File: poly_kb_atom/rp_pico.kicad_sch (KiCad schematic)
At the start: 44 parts, among them SW2 TSA343G00-250J2, SW3 TSA343G00-250J2, U1 TD6811, U10 RP2040, U9 W25Q64JVSSIQ, Y1 TAXM12M4RFBCCT2T

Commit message: Current production version of right side and added STLs
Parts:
- C15, C16, C17, C18, C19, C20, C21, C22, C23, C7, C9: LCSC C1525 -> (none); MPN CL05B104KO5NNNC -> C1525
- C24, C25: LCSC C52923 -> (none); MPN CL05A105KA5NQNC -> C52923
- C26, C4, C6: LCSC C15850 -> (none); MPN CL21A106KAYNNNE -> C15850
- C3, C8: LCSC C1557 -> (none); MPN 0402CG270J500NT -> C1557
- C5: LCSC C1653 -> (none); MPN CL10C220JB8NNNC -> C1653
- CR1: LCSC C8598 -> (none); MPN B5819W SL -> C8598
- D1: LCSC C84256 -> (none); MPN NCD0805R1 -> C84256
- L2: LCSC C2836880 -> (none); MPN MCS0530-4R7MN2 -> C2836880
- R14: LCSC C23150 -> (none); MPN (none) -> C25822
- R15, R20: LCSC C25744 -> (none); MPN (none) -> C25744
- R16, R19: LCSC C21190 -> (none); MPN (none) -> C21190
- R17: LCSC C22807 -> (none); MPN (none) -> C22807
- R18: LCSC C25091 -> (none); MPN (none) -> C25091
- R21: value 1K 0603 -> 1K 0402; LCSC C21190 -> (none); MPN (none) -> C11702
- R22, R23: LCSC C25190 -> (none); MPN (none) -> C25190
- R7, R9: LCSC C25905 -> (none); MPN (none) -> C25905
- R8: LCSC C25908 -> (none); MPN (none) -> C25908
- SW2, SW3: value TSA343G00-250J2 -> EVQPUC02K; LCSC C79174 -> (none); MPN EVQPUC02K -> C79174
- U1: LCSC C189486 -> (none); MPN TD6811 -> C189486
- U10: LCSC C2040 -> (none); MPN (none) -> C2040
- U9: LCSC C179171 -> (none); MPN W25Q64JVSSIQ -> C179171
- USB1: LCSC C165948 -> (none); MPN TYPE-C-31-M-12 -> C165948
- Y1: LCSC C133337 -> (none); MPN TAXM12M4RFBCCT2T -> C133337

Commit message: Backup before moving to Kicad7
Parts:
- removed C7: 100nF 0402 16V, Capacitor_SMD:C_0402_1005Metric, symbol Device:C_Small
- removed CR1: B5819W SL, Diode_SMD:D_SOD-123, symbol rpi-pico-debugger-shoe-rescue:MBR120VLSFT1G-2021-05-12_00-49-18
- removed R18: 220 0402, Resistor_SMD:R_0402_1005Metric, symbol Device:R
- added D2: ESD5Z5V0, Diode_SMD:D_SOD-523, symbol Diode:SMF6V0A
- added F2: SMD0805-050-16V, Fuse:Fuse_1206_3216Metric, symbol Device:Fuse
- added FB3: GZ2012D601TF, Inductor_SMD:L_0805_2012Metric, symbol Device:FerriteBead_Small
- added R18: 10M 0603, Resistor_SMD:R_0603_1608Metric, symbol Device:R_Small
- added R24: 2M2 0603, Resistor_SMD:R_0603_1608Metric, symbol Device:R_Small
- added U13: TPD4E05U06DQAR, poly_kb:USON-10, symbol acheron_Symbols:TPD4E05U06DQAR
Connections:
- net GND: now also SW2.1, D2.2 (A2), FB3.2, R24.2, U13.3 (GND), U13.8 (GND); no longer SW2.2
- net USB_D+: now also U13.1 (IO1), U13.10 (NC), U13.4 (D2+), U13.7 (NC)
- net USB_D-: now also U13.2 (IO2), U13.5 (D2-), U13.6 (NC), U13.9 (NC)
- net VBUS: now also D2.1 (A1), F2.1; no longer R8.1
- net VSYS: now also R8.1, F2.2
- net ~{USB_BOOT}: now also SW2.2; no longer SW2.1
- net at USB1.13 (SHIELD): now also FB3.1
- net at C5.2, R14.1, R17.2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: now also R18.1
- new net: R18.2, R24.1
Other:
- note added: "ESD"
- note added: "If USB is the only power source it is safe to use VBUS=VSYS, otherwise we need no insert a Schottky barrier diode in-between."
- note added: "R1"
- note added: "R2"
- note added: "Vout = 0.6*(1+R2/R1)"
- moved on the sheet: C9, R14, R15, R17, R20, R21, R8, SW2, U9

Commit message: Revised Rev2
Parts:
- removed U1: TD6811, Package_TO_SOT_SMD:TSOT-23-5, symbol poly_kb:TD6811
- added U2: TD6811, Package_TO_SOT_SMD:TSOT-23-5, symbol poly_kb:TD6811
- F2: value SMD0805-050-16V -> 2920L030DR; footprint Fuse:Fuse_1206_3216Metric -> Fuse:Fuse_2920_7451Metric; LCSC Part Number C2833485 -> (none); MPN (none) -> C207081; Manufacturer TECHFUSE -> (none); Manufacturer Part Number SMD0805-050-16V -> (none); Package F0805 -> (none)
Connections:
- net GND: now also U2.2 (GND)
- net VSYS: now also U2.1 (RUN), U2.4 (VDD)
- net at L2.1: now also U2.3 (SW)
- net at C5.2, R14.1, R17.2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: now also U2.5 (FB)
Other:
- note added: "IHold = 300mA, ITrip = 600 mA"

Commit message: Right side: Production version Rev2
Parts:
- removed U9: W25Q64JVSSIQ, Package_SO:SOIC-8_5.275x5.275mm_P1.27mm, symbol rpi-pico-debugger-shoe-rescue:W25Q16JVSSIQ-W25Q16JVSSIQ
- added U9: W25Q64JVXGIQ, SON80P400X400X50-9N, symbol Winbond Flash:W25Q64JVXGIQ
- D1: value Red 0805 -> Red 0805 C84256
- U13: Package uSON-10 -> (none)
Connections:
- net 3V3: now also U9.8 (VCC)
- net GND: now also U9.4 (GND), U9.9 (EP)
- net QSPI_SCLK: now also U9.6 (CLK)
- net QSPI_SD0: now also U9.5 (DI(IO0))
- net QSPI_SD1: now also U9.2 (DO(IO1))
- net QSPI_SD2: now also U9.3 (~{WP(IO2}))
- net QSPI_SD3: now also U9.7 (~{HOLD_OR_}RESET_(IO3))
- net QSPI_SS: now also U9.1 (~{CS})
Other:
- moved on the sheet: C9, R20, R21, SW2

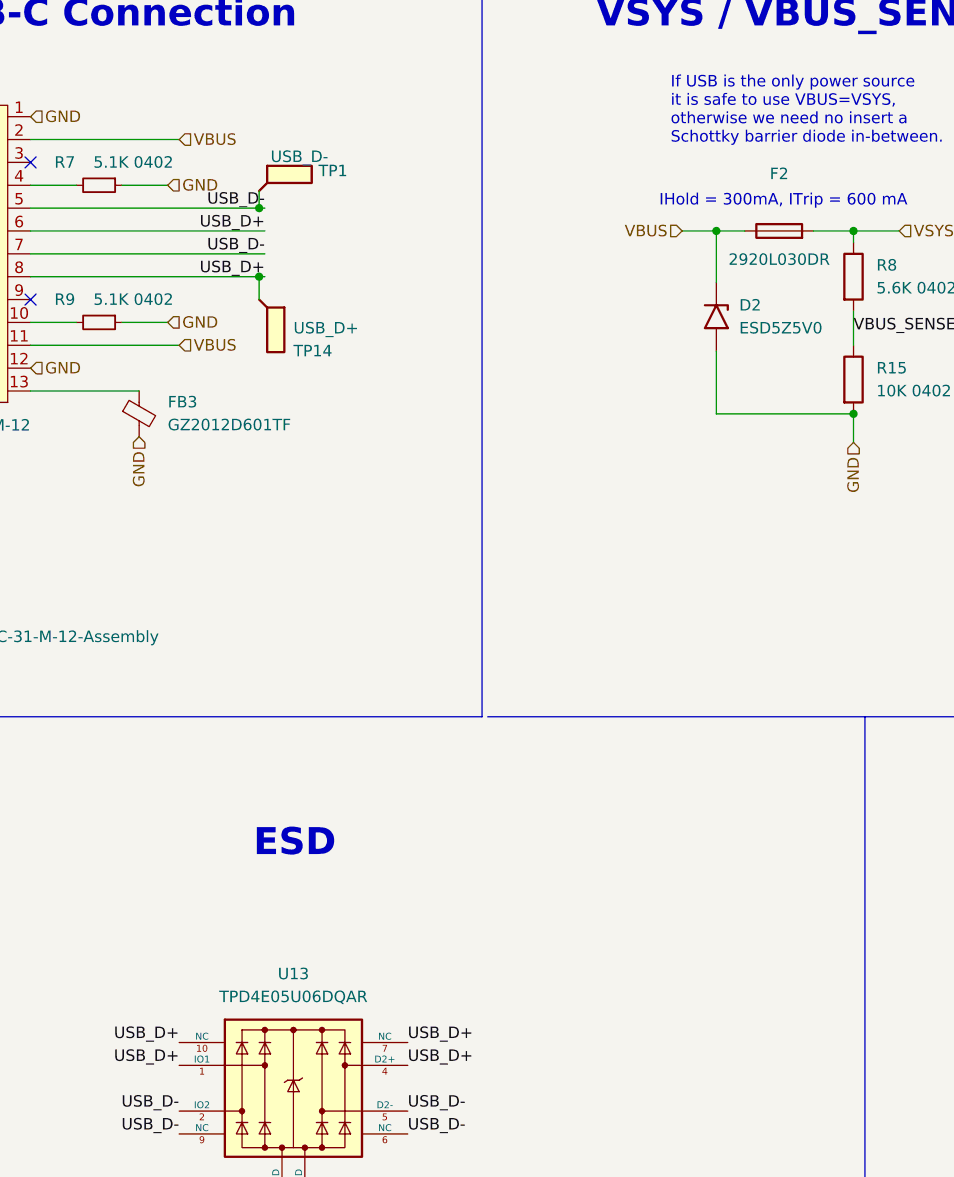
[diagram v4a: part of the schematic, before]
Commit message: Updated all openSCAD models and various fixes for the right side before final production
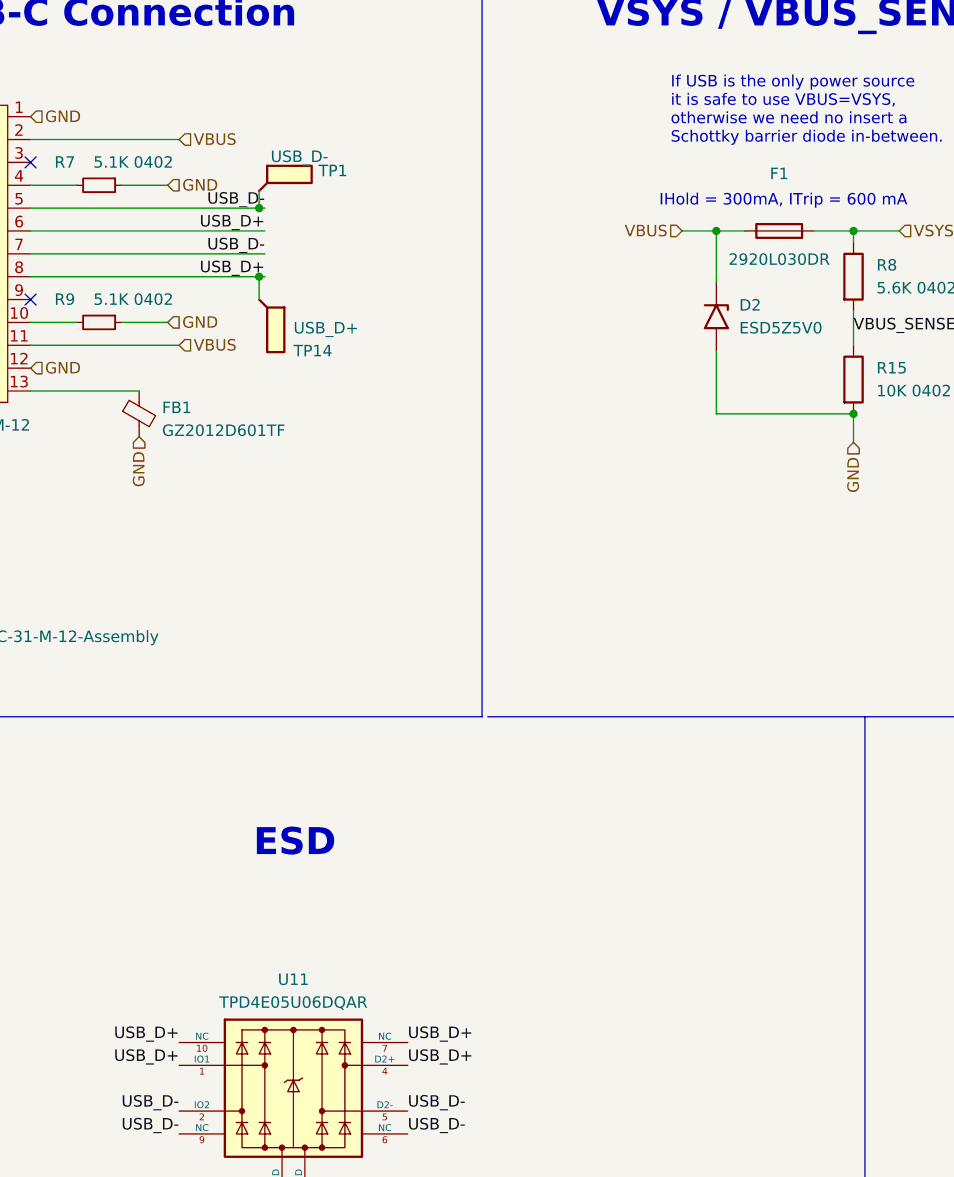
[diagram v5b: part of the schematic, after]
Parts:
- renumbered F2 to F1, FB3 to FB1, U13 to U11
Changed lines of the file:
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@@
   (title_block
     (title "rp2040 base circuit")
+    (date "2023-03-09")
   )
   (junction (at 337.82 78.74) (diameter 0) (color 0 0 0 0)
@@
   (symbol (lib_id "acheron_Symbols:TPD4E05U06DQAR") (at 69.215 145.415 0) (unit 1)
     (in_bom yes) (on_board yes) (dnp no) (fields_autoplaced)
-    (property "Reference" "U13" (at 69.215 132.715 0)
-      (effects (font (size 1.27 1.27)))
-    )
-    (property "Value" "TPD4E05U06DQAR" (at 69.215 135.255 0)
+    (property "Reference" "U11" (at 69.215 133.35 0)
+      (effects (font (size 1.27 1.27)))
+    )
+    (property "Value" "TPD4E05U06DQAR" (at 69.215 135.89 0)
       (effects (font (size 1.27 1.27)))
     )
@@
       (project "poly_kb_wave_right2"
         (path "/e63e39d7-6ac0-4ffd-8aa3-1841a4541b55/5b575f2a-a831-41f0-985e-3d214d07238c"
-          (reference "U13") (unit 1)
+          (reference "U11") (unit 1)
         )
       )
@@
   (symbol (lib_id "Device:FerriteBead_Small") (at 52.07 70.485 0) (unit 1)
     (in_bom yes) (on_board yes) (dnp no) (fields_autoplaced)
-    (property "Reference" "FB3" (at 55.245 69.1768 0)
-      (effects (font (size 1.27 1.27)) (justify left))
-    )
-    (property "Value" "GZ2012D601TF" (at 55.245 71.7168 0)
+    (property "Reference" "FB1" (at 54.61 69.8119 0)
+      (effects (font (size 1.27 1.27)) (justify left))
+    )
+    (property "Value" "GZ2012D601TF" (at 54.61 72.3519 0)
       (effects (font (size 1.27 1.27)) (justify left))
     )
@@
       (project "poly_kb_wave_right2"
         (path "/e63e39d7-6ac0-4ffd-8aa3-1841a4541b55/5b575f2a-a831-41f0-985e-3d214d07238c"
-          (reference "FB3") (unit 1)
+          (reference "FB1") (unit 1)
         )
       )
@@
   (symbol (lib_id "Device:Fuse") (at 123.19 50.165 90) (unit 1)
     (in_bom yes) (on_board yes) (dnp no)
-    (property "Reference" "F2" (at 123.19 43.815 90)
+    (property "Reference" "F1" (at 123.19 43.815 90)
       (effects (font (size 1.27 1.27)))
     )
@@
       (project "poly_kb_wave_right2"
         (path "/e63e39d7-6ac0-4ffd-8aa3-1841a4541b55/5b575f2a-a831-41f0-985e-3d214d07238c"
-          (reference "F2") (unit 1)
-        )
-      )
+          (reference "F1") (unit 1)
+        )
+      )
